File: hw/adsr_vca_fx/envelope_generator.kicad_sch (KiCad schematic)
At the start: 11 parts, among them J8 Conn_02x05_Odd_Even, SW3 SW_Push, SW4 SW_Push, U5 STM32L432KBUx

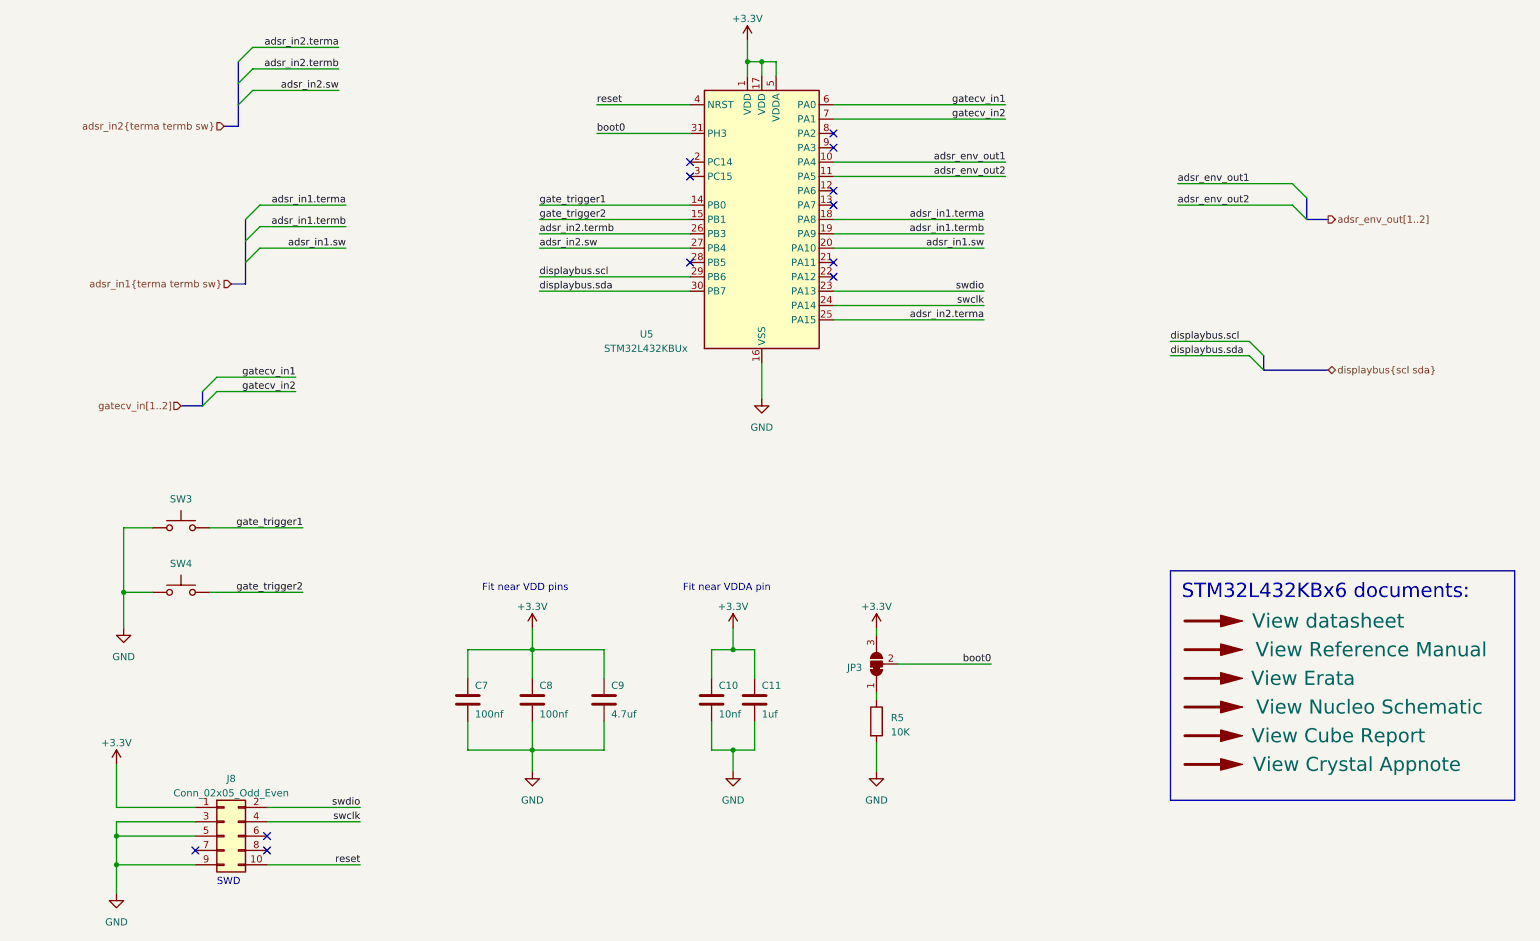
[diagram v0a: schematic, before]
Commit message: modified design into normal/inverted envlope
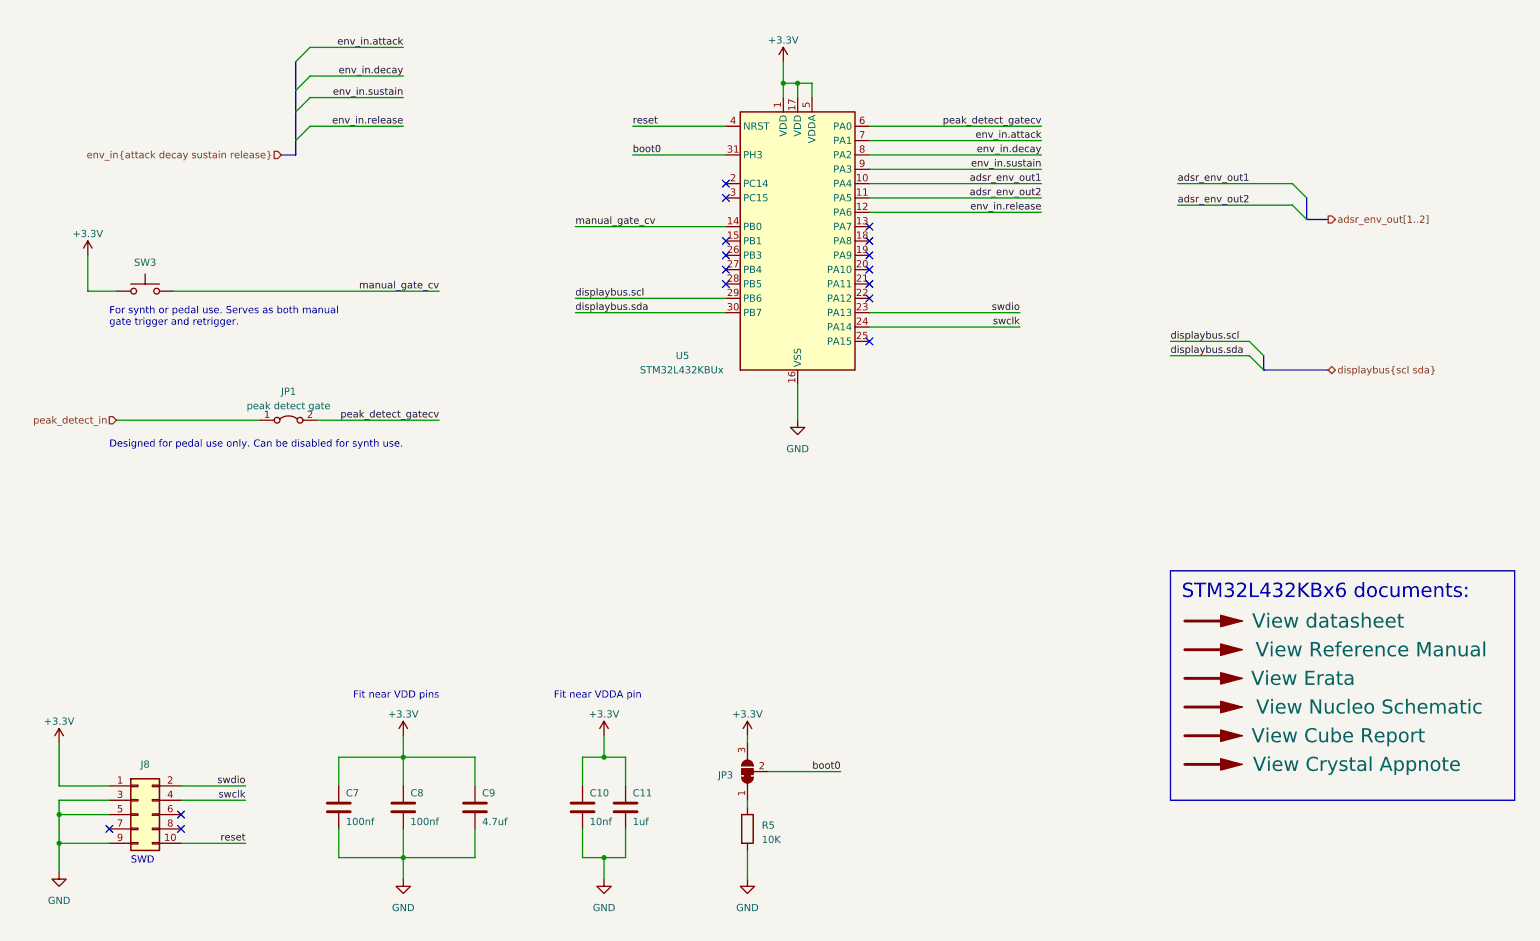
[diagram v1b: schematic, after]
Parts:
- removed SW4: SW_Push, Button_Switch_THT:SW_PUSH_6mm, symbol Switch:SW_Push
- added JP1: peak detect gate, Connector_PinSocket_2.54mm:PinSocket_1x02_P2.54mm_Vertical, symbol Jumper:Jumper_2_Bridged
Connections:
- net +3.3V: now also SW3.1
- net GND: no longer SW3.1
- net env_in.release: now reaches U5.12 (PA6)
- net env_in.decay: now reaches U5.8 (PA2)
- net env_in.sustain: now reaches U5.9 (PA3)
- net adsr_in1.sw: no longer names the net of U5.20 (PA10)
- net adsr_in1.terma: no longer names the net of U5.18 (PA8)
- net adsr_in1.termb: no longer names the net of U5.19 (PA9)
- net adsr_in2.sw: no longer names the net of U5.27 (PB4)
- net adsr_in2.terma: no longer names the net of U5.25 (PA15)
- net adsr_in2.termb: no longer names the net of U5.26 (PB3)
- net gate_trigger1 renamed manual_gate_cv
- net gate_trigger2: no longer names the net of U5.15 (PB1)
- net gatecv_in1 renamed peak_detect_gatecv
- net peak_detect_gatecv: now also JP1.2 (B)
- net gatecv_in2 renamed env_in.attack
- new net peak_detect_in: JP1.1 (A)
- no-connect marks 12 -> 16
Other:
- note added: "Designed for pedal use only. Can be disabled for synth use."
- note added: "For synth or pedal use. Serves as both manual gate trigger and retrigger."
- moved on the sheet: C10, C11, C7, C8, C9, J8, JP3, R5, SW3, U5

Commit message: first draft layout
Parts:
- renumbered C7 to C5, C8 to C6, C9 to C7, C10 to C8, C11 to C9, J8 to J6, JP3 to JP2, R5 to R6, SW3 to SW1, U5 to U3

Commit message: tidied up layout
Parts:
- removed JP2: SolderJumper_3_Bridged12, Jumper:SolderJumper-3_P1.3mm_Bridged12_Pad1.0x1.5mm, symbol Jumper:SolderJumper_3_Bridged12
- added J12: Conn_01x03, Connector_PinHeader_2.54mm:PinHeader_1x03_P2.54mm_Vertical, symbol Connector_Generic:Conn_01x03
- JP1: footprint Connector_PinSocket_2.54mm:PinSocket_1x02_P2.54mm_Vertical -> Connector_PinHeader_2.54mm:PinHeader_1x02_P2.54mm_Vertical
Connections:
- net +3.3V: now also J12.3 (Pin_3)
- net boot0: now also J12.2 (Pin_2)
- net at R6.1: now also J12.1 (Pin_1)
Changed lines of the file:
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@@
     (stroke (width 0) (type default))
   )
-  (wire (pts (xy 146.05 162.56) (xy 146.05 163.83))
+  (wire (pts (xy 144.78 154.94) (xy 146.05 154.94))
+    (stroke (width 0) (type default))
+  )
+  (wire (pts (xy 146.05 160.02) (xy 146.05 163.83))
     (stroke (width 0) (type default))
   )
@@
     (stroke (width 0) (type default))
   )
-  (wire (pts (xy 149.86 157.48) (xy 162.56 157.48))
+  (wire (pts (xy 144.78 157.48) (xy 162.56 157.48))
     (stroke (width 0) (type default))
   )
@@
     (stroke (width 0) (type default))
   )
-  (wire (pts (xy 146.05 151.13) (xy 146.05 152.4))
+  (wire (pts (xy 146.05 151.13) (xy 146.05 154.94))
     (stroke (width 0) (type default))
   )
@@
   )
   (bus (pts (xy 245.11 55.88) (xy 245.11 59.69))
+    (stroke (width 0) (type default))
+  )
+  (wire (pts (xy 146.05 160.02) (xy 144.78 160.02))
     (stroke (width 0) (type default))
   )
@@
         (path "/2c7cc946-dcca-4ffb-b6a0-bf0c9ddb491b/1d3f5b6b-6d64-41ce-b32c-1d62b69c11ca"
           (reference "#PWR033") (unit 1)
-        )
-      )
-    )
-  )
-  (symbol (lib_id "Jumper:SolderJumper_3_Bridged12") (at 146.05 157.48 90) (unit 1)
-    (in_bom yes) (on_board yes) (dnp no) (fields_autoplaced)
-    (property "Reference" "JP2" (at 143.51 158.115 90)
-      (effects (font (size 1.27 1.27)) (justify left))
-    )
-    (property "Value" "SolderJumper_3_Bridged12" (at 143.51 159.385 90)
-      (effects (font (size 1.27 1.27)) (justify left) hide)
-    )
-    (property "Footprint" "Jumper:SolderJumper-3_P1.3mm_Bridged12_Pad1.0x1.5mm" (at 146.05 157.48 0)
-      (effects (font (size 1.27 1.27)) hide)
-    )
-    (property "Datasheet" "~" (at 146.05 157.48 0)
-      (effects (font (size 1.27 1.27)) hide)
-    )
-    (pin "1")
-    (pin "2")
-    (pin "3")
-    (instances
-      (project "adsr_vca_fx"
-        (path "/2c7cc946-dcca-4ffb-b6a0-bf0c9ddb491b/1d3f5b6b-6d64-41ce-b32c-1d62b69c11ca"
-          (reference "JP2") (unit 1)
         )
       )
@@
       (effects (font (size 1.27 1.27)))
     )
-    (property "Footprint" "Connector_PinSocket_2.54mm:PinSocket_1x02_P2.54mm_Vertical" (at 64.77 95.25 0)
+    (property "Footprint" "Connector_PinHeader_2.54mm:PinHeader_1x02_P2.54mm_Vertical" (at 64.77 95.25 0)
       (effects (font (size 1.27 1.27)) hide)
     )
@@
         )
       )
+    )
+  )
+  (symbol (lib_id "Connector_Generic:Conn_01x03") (at 139.7 157.48 180) (unit 1)
+    (in_bom yes) (on_board yes) (dnp no)
+    (property "Reference" "J12" (at 139.7 162.56 0)
+      (effects (font (size 1.27 1.27)))
+    )
+    (property "Value" "Conn_01x03" (at 139.7 162.56 0)
+      (effects (font (size 1.27 1.27)) hide)
+    )
+    (property "Footprint" "Connector_PinHeader_2.54mm:PinHeader_1x03_P2.54mm_Vertical" (at 139.7 157.48 0)
+      (effects (font (size 1.27 1.27)) hide)
+    )
+    (property "Datasheet" "~" (at 139.7 157.48 0)
+      (effects (font (size 1.27 1.27)) hide)
+    )
+    (pin "1")
+    (pin "2")
+    (pin "3")
+    (instances
+      (project "adsr_vca_fx"
+        (path "/2c7cc946-dcca-4ffb-b6a0-bf0c9ddb491b/1d3f5b6b-6d64-41ce-b32c-1d62b69c11ca"
+          (reference "J12") (unit 1)
+        )
+      )

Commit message: updated layout
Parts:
- U3: footprint Package_DFN_QFN:QFN-32-1EP_5x5mm_P0.5mm_EP3.45x3.45mm -> Package_DFN_QFN:QFN-32-1EP_5x5mm_P0.5mm_EP3.45x3.45mm_ThermalVias
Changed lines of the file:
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@@
       (effects (font (size 1.27 1.27)) (justify left))
     )
-    (property "Footprint" "Package_DFN_QFN:QFN-32-1EP_5x5mm_P0.5mm_EP3.45x3.45mm" (at 144.78 86.36 0)
+    (property "Footprint" "Package_DFN_QFN:QFN-32-1EP_5x5mm_P0.5mm_EP3.45x3.45mm_ThermalVias" (at 144.78 86.36 0)
       (effects (font (size 1.27 1.27)) (justify right) hide)
     )
